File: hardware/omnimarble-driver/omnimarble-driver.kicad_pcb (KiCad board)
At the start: 4 copper layers, 220 x 150 mm, 178 parts, among them J1 24V-IN, J10 PICO-SOCKET, J11 IO-BREAKOUT, J2 AUX-BANK, J3 E-STOP-NC, J4 ARM-KEY, J5 COIL, J6 RAIL-EMIT, J7 RAIL-RECV, J8 SPARE-JST, J9 PICO-SOCKET, K1 HF3FF-12V, K2 HF3FF-12V, Q1 MMBT3904, Q10 SFT040N150C3, Q11 SFT040N150C3, Q12 SFT040N150C3, Q2 MMBT3904, Q3 MMBT3904, Q4 MMBT3904, Q90 AOD4185, Q91 AOD66923, U1 AP63205, U10 ADS7042, U11 LM339, U12 LM339, U2 78L12, U3 MCP6002, U4 UC3843B, U5 CJ431-0.5%, U6 74LVC1G08, U7 UCC27524A, U8 UCC27524A, U9 INA240A1

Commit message: Driver PCB: fix BST_G boost-gate placement (37.8mm -> 3.6mm)
Targeted critical-net fix from the routing-quality review. R6 (boost gate
resistor) was ~19mm from Q91's gate despite its "beside Q91" comment, giving a
37.8mm BST_G loop (ratio 1.9). Moved R6 above Q91 (clear of L2/R7) so
pad2(BST_G) is 3.3mm from Q91.G -> BST_G now 3.6mm, ratio 1.1 (direct, F.Cu
only, source-referenced). DRV1 also improved (1.9->1.5); BOOST_EN_N/VSET_PWM
now connected + direct.

Board: 0 shorts/clearance/parity/courtyard, 11 unconnected (freerouting
congestion in dense areas), 2 text_height, 1 via_dangling. NOTE: repair-mode
A* is counterproductive on a freerouted board (coarse grid vs FR's dense copper
-> shorts); the last unconnected need GUI push-and-shove or explicit traces.

Co-Authored-By: Claude Fable 5 <noreply@anthropic.com>
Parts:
- moved R6 22.7 mm to (48.5, 93.8)
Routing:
- net ESTOP_SENSE: track 249.7 -> 63.4 mm, vias 3 -> 0
- net VSET_PWM: track 52.3 -> 197.5 mm, vias 1 -> 5
- net BOOST_EN_N: track 48.0 -> 146.7 mm, vias 1 -> 3
- net BST_FB: track 135.7 -> 47.3 mm, vias 7 -> 0
- net CIN3: track 67.0 -> 12.3 mm, vias 4 -> 0
- net 3V3: track 327.5 -> 371.7 mm, vias 7 -> 11
- net BST_G: track 37.8 -> 3.59 mm
- net SIG3: track 154.3 -> 130.0 mm, vias 3 -> 2
- net BST_COMP: track 50.3 -> 26.2 mm
- net +12V: track 199.8 -> 222.1 mm, vias 5 -> 2
- net K2_COIL: track 105.3 -> 85.4 mm, vias 2 -> 1
- net +5V: track 457.7 -> 437.8 mm, vias 5 -> 4
- net VBANK_DIV: track 7.87 -> 26.6 mm
- net BST_DRV: track 14.4 -> 31.5 mm
- net GATE3: track 162.2 -> 178.6 mm, vias 4 -> 6
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
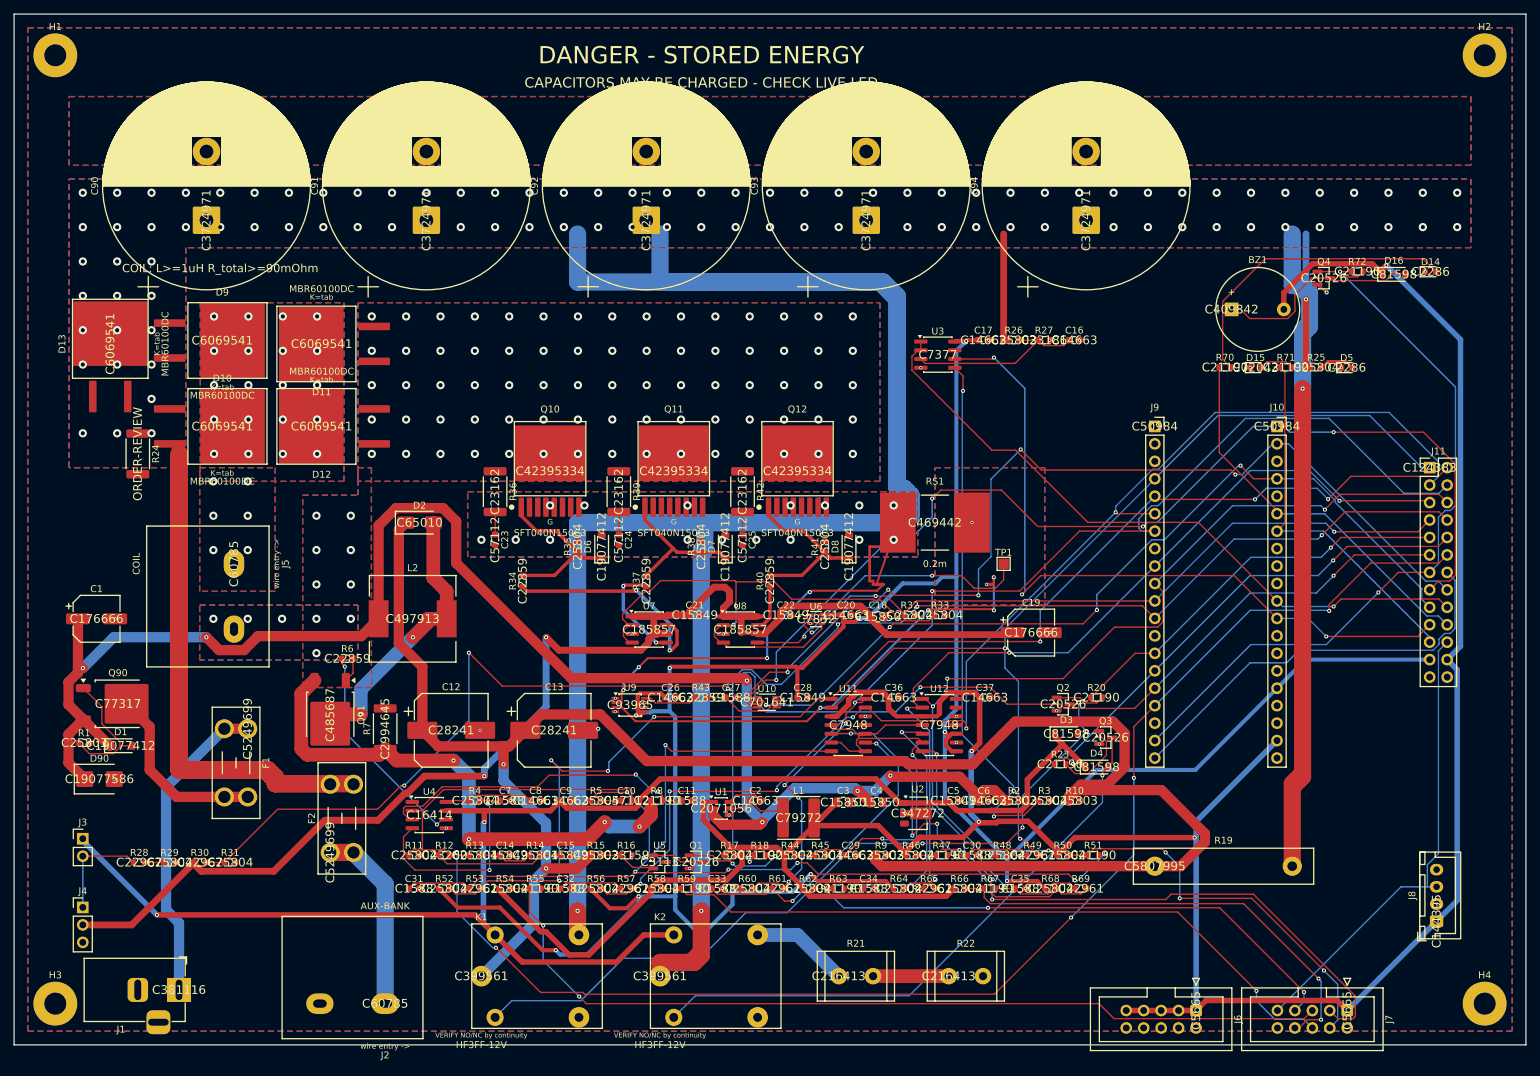
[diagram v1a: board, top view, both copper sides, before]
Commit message: Driver PCB: remove J11 IO-breakout + GND-pour tuning (unconnected 11->9)
Per design review: the 2x13 J11 breakout duplicated all 26 control/sense nets
(GATE1-6, MCU_FIRE, ARM/ESTOP, ADC SPI, boost EN/PWM, ...) into the congested
MCU/sense area, doubling the routing burden there. Removed it; MCU-agnostic
access is preserved via the Pico socket pins (J9/J10) for a Pico-form-factor
carrier or jumpers. Netlist drops from 265->241 preroute airwires.

- gen_schematic.py: J11 removed; .kicad_pro now written WITH board design
  rules (min via 0.4 / hole 0.2 / hole-to-hole 0.25) so kicad-cli DRC uses
  them instead of KiCad's stricter defaults after every regen.
- gen_pcb.py build_zones: F/B GND pour clearance 0.3->0.2, min_thick
  0.25->0.13 so the pour flows into narrow necks and reaches isolated GND pads.

Board (220mm, both GND planes): 0 shorts/clearance/parity, 9 unconnected
(2 GND + 3V3 x2 + SW_DRAIN/VBOOST/+24V/BSTINH_B/VSET_PWM), 2 cosmetic
text_height, 1 via_dangling.

Co-Authored-By: Claude Fable 5 <noreply@anthropic.com>
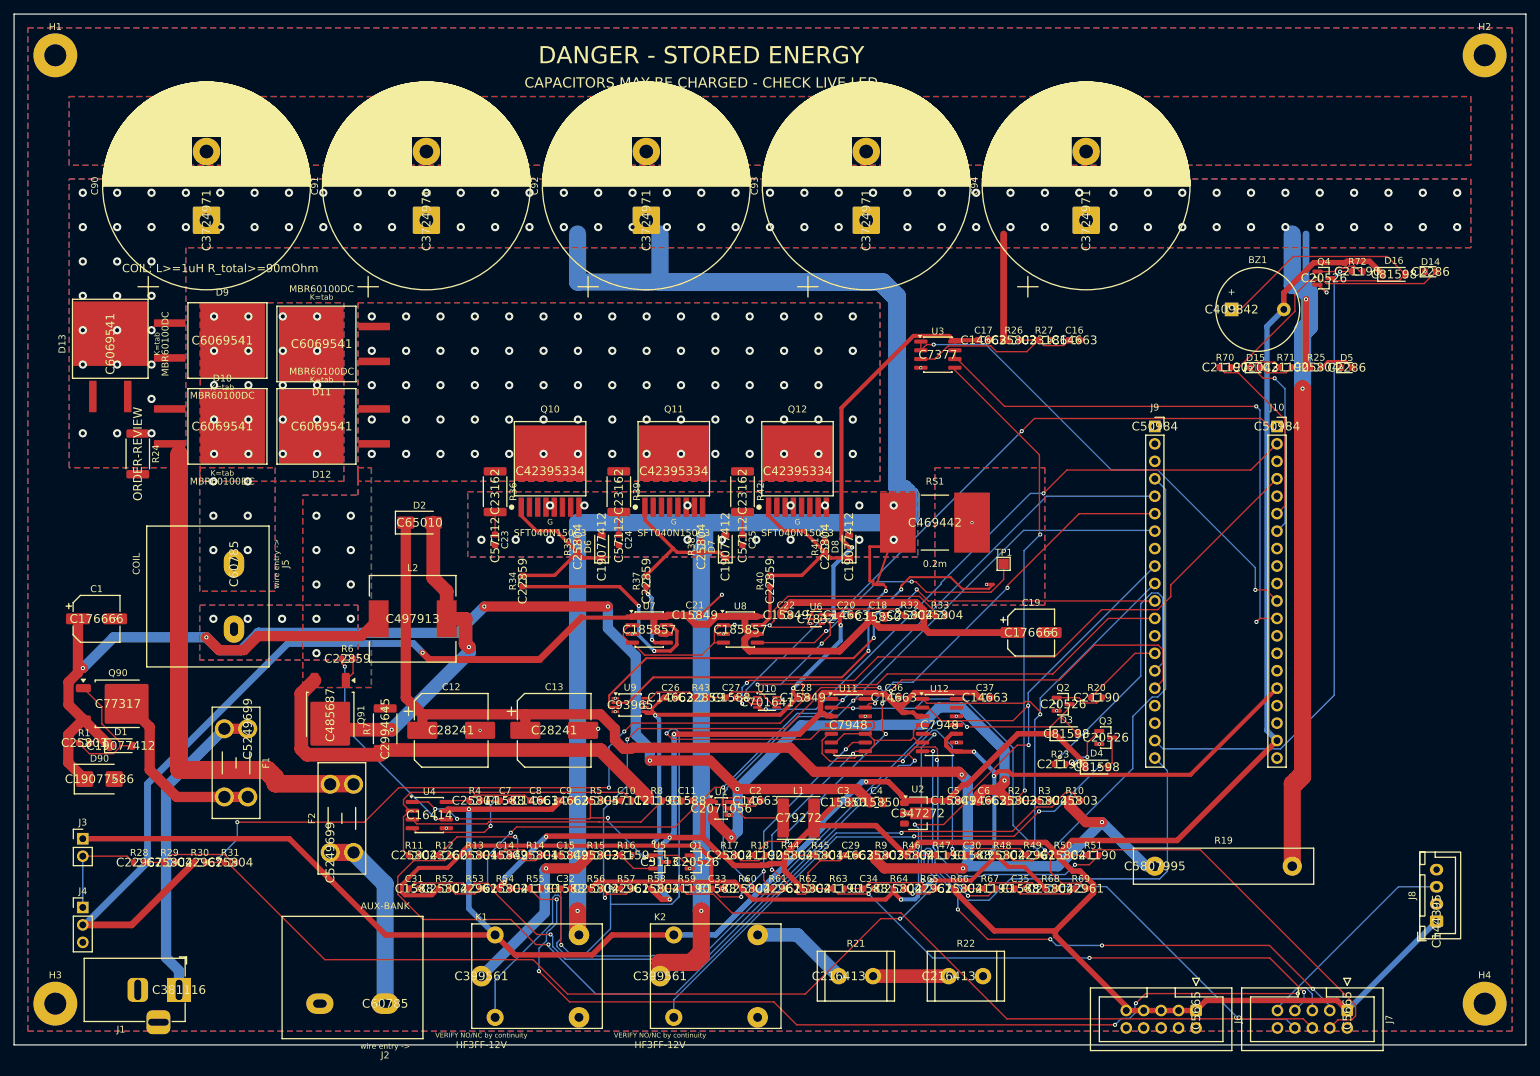
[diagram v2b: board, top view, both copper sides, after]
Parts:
- removed J11: IO-BREAKOUT, Connector_PinHeader_2.54mm:PinHeader_2x13_P2.54mm_Vertical
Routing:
- net VSET_PWM: track 197.5 -> 0.00 mm, vias 5 -> 0
- net ESTOP_SENSE: track 63.4 -> 195.6 mm, vias 0 -> 1
- net BST_FB: track 47.3 -> 174.6 mm, vias 0 -> 2
- net CIN3: track 12.3 -> 94.4 mm, vias 0 -> 3
- net VBOOST: track 281.0 -> 211.0 mm, vias 2 -> 4
- net GATE6: track 143.0 -> 76.0 mm, vias 4 -> 2
- net BOOST_EN_N: track 146.7 -> 83.0 mm, vias 3 -> 4
- net GATE2: track 189.4 -> 131.4 mm, vias 7 -> 4
- net GATE4: track 157.0 -> 101.4 mm, vias 6 -> 2
- net ADC_SDO: track 152.3 -> 97.5 mm, vias 4 -> 2
- net GATE3: track 178.6 -> 125.8 mm, vias 6 -> 5
- net MCU_FIRE: track 103.7 -> 53.9 mm, vias 3 -> 2
- net ADC_CS: track 141.5 -> 91.8 mm, vias 5 -> 2
- net RLY_CHARGE: track 59.0 -> 12.0 mm, vias 1 -> 0
- net 3V3: track 371.7 -> 326.2 mm
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
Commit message: DeepPCB-ready DSN: fit all track widths to pads (no neck-down needed)
DeepPCB (unlike freerouting) refuses to neck a track down at a pad, flagging
ROUTING_UNROUTABLE_PIN_TRACKWIDTH_EXCEEDS_PIN_SIZE. Narrowed every routed net
whose class width exceeded its smallest connected pad: +24V/+12V/+12V_SW/+5V
0.5, 3V3 0.3, VBOOST/BST_CS_HI/VBANK 0.7, BST_SW 1.5. All low-current
control/sense/logic taps (the pulse path is unaffected pours). Plane nets
carry current in the polygon, not the routed tap. Verified: no net's class
width exceeds any of its pads. Combined with the unconnected-() name sanitizer,
the DSN now parses and routes cleanly in DeepPCB.

Co-Authored-By: Claude Fable 5 <noreply@anthropic.com>
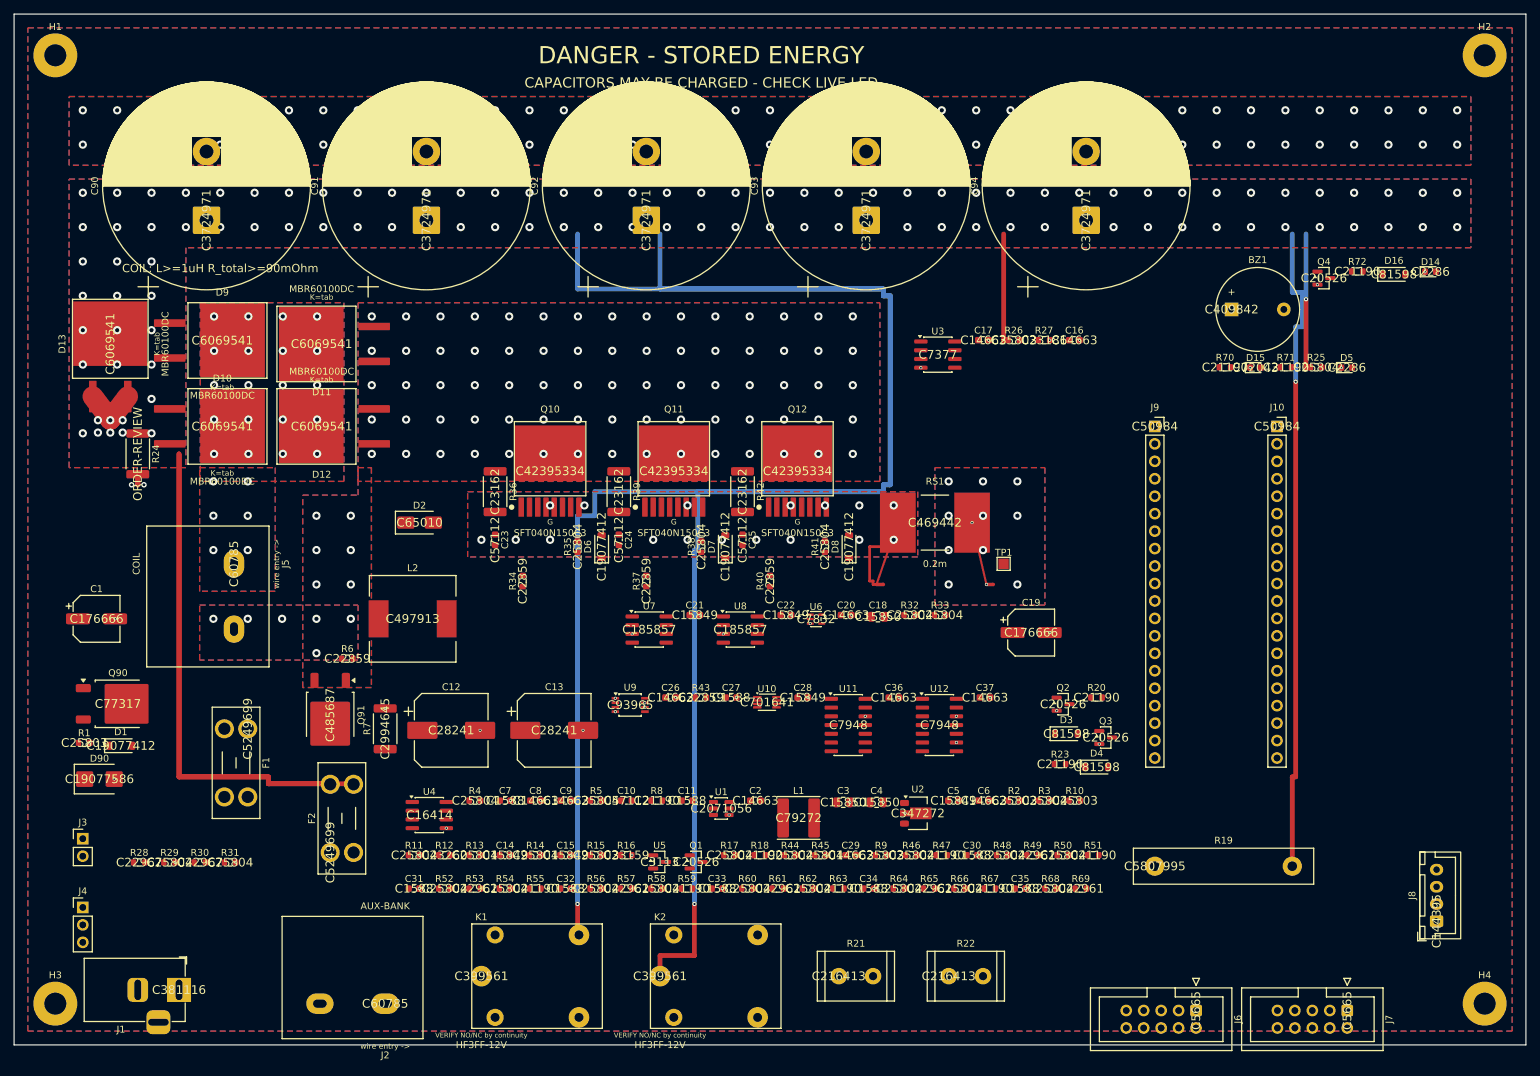
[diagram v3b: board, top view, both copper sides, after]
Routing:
- net +5V: track 420.9 -> 0.00 mm, vias 5 -> 0
- net 3V3: track 326.2 -> 0.00 mm, vias 11 -> 0
- net +24V: track 273.2 -> 0.00 mm, vias 8 -> 0
- net +12V_SW: track 227.3 -> 0.00 mm, vias 1 -> 0
- net +12V: track 212.1 -> 0.00 mm, vias 2 -> 0
- net VBOOST: track 211.0 -> 0.00 mm, vias 4 -> 0
- net ESTOP_SENSE: track 195.6 -> 0.00 mm, vias 1 -> 0
- net ARM_SENSE: track 185.4 -> 0.00 mm, vias 6 -> 0
- net BST_FB: track 174.6 -> 0.00 mm, vias 2 -> 0
- net CIN2: track 151.8 -> 0.00 mm, vias 4 -> 0
- net SIG3: track 140.6 -> 0.00 mm, vias 5 -> 0
- net GATE2: track 131.4 -> 0.00 mm, vias 4 -> 0
- net GATE3: track 125.8 -> 0.00 mm, vias 5 -> 0
- net K1_COIL: track 124.6 -> 0.00 mm, vias 1 -> 0
- net GATE1: track 117.2 -> 0.00 mm, vias 2 -> 0
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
